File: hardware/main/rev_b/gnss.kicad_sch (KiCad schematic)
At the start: 22 parts, among them J30 GNSS_UFL, Q30 2N7002, U30 LG77LICMD

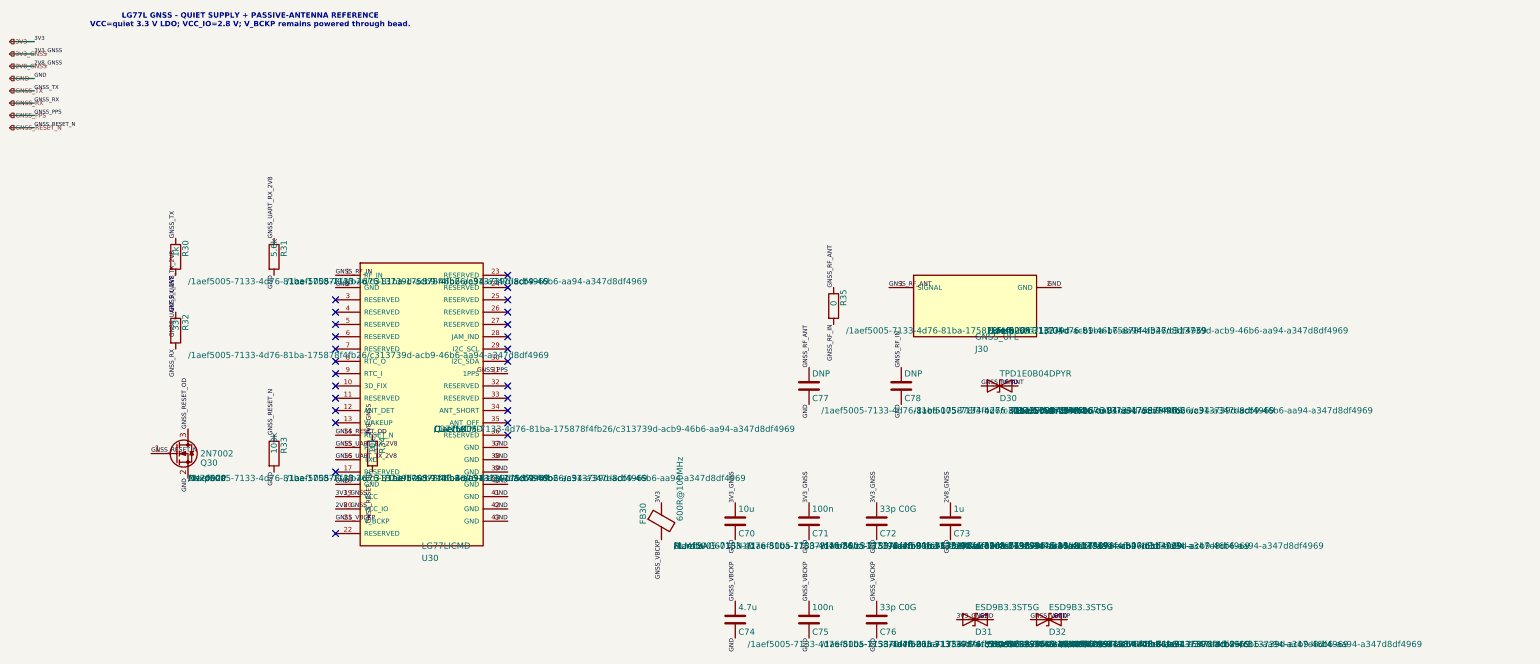
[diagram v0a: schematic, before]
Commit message: fix: consolidate portable Rev-B hardware sources
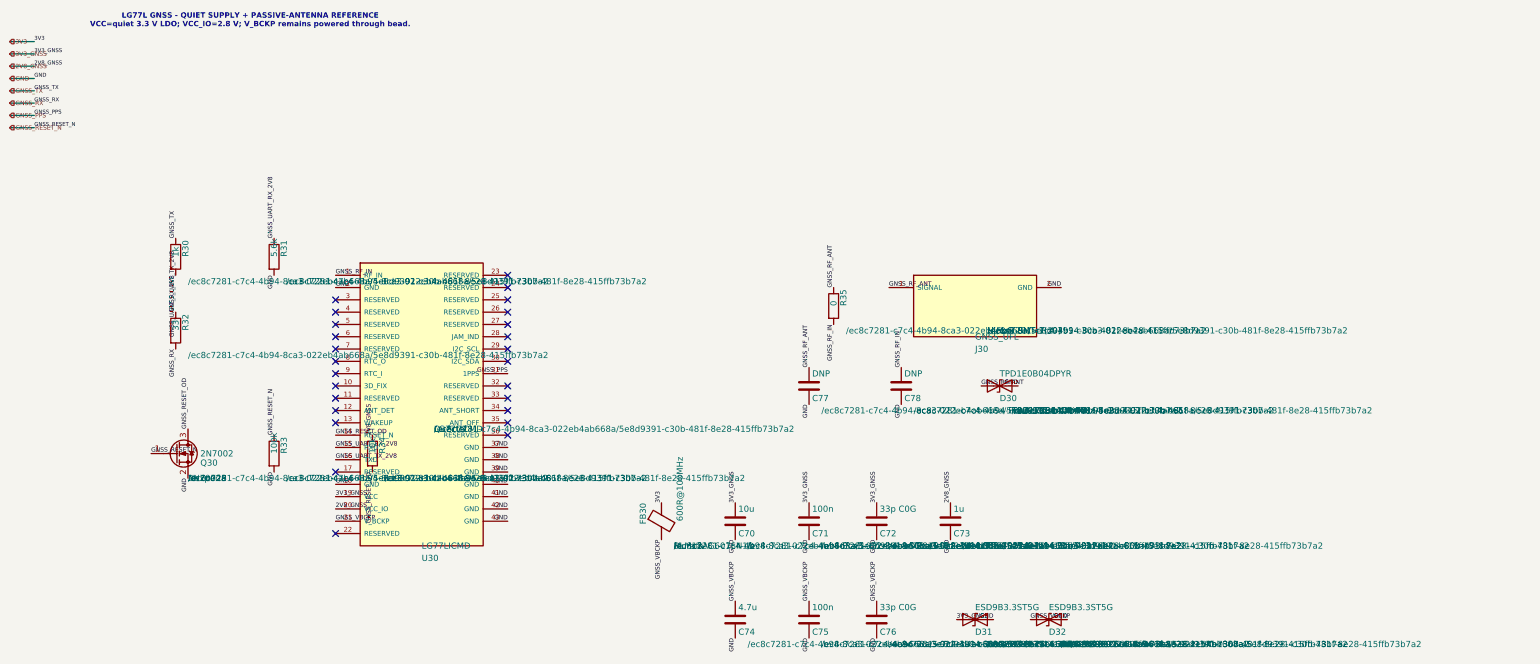
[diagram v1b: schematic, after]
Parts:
- C70, C71, C72, C73, C74, C75, C76, C77, C78, D30, D31, D32, FB30, J30, Q30, R30, R31, R32, R33, R34, R35, U30: hierarchy_path /1aef5005-7133-4d76-81ba-175878f4fb26/c313739d-acb9-46b6-aa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 -> /ec8c7281-c7c4-4b94-8ca3-022eb4ab668a/5e8d9391-c30b-481f-8e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
